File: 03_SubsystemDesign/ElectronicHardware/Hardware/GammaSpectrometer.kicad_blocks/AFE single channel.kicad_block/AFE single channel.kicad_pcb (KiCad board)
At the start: 4 copper layers, 29 parts, among them U2101 OPA690xDBV, U2102 AD8139

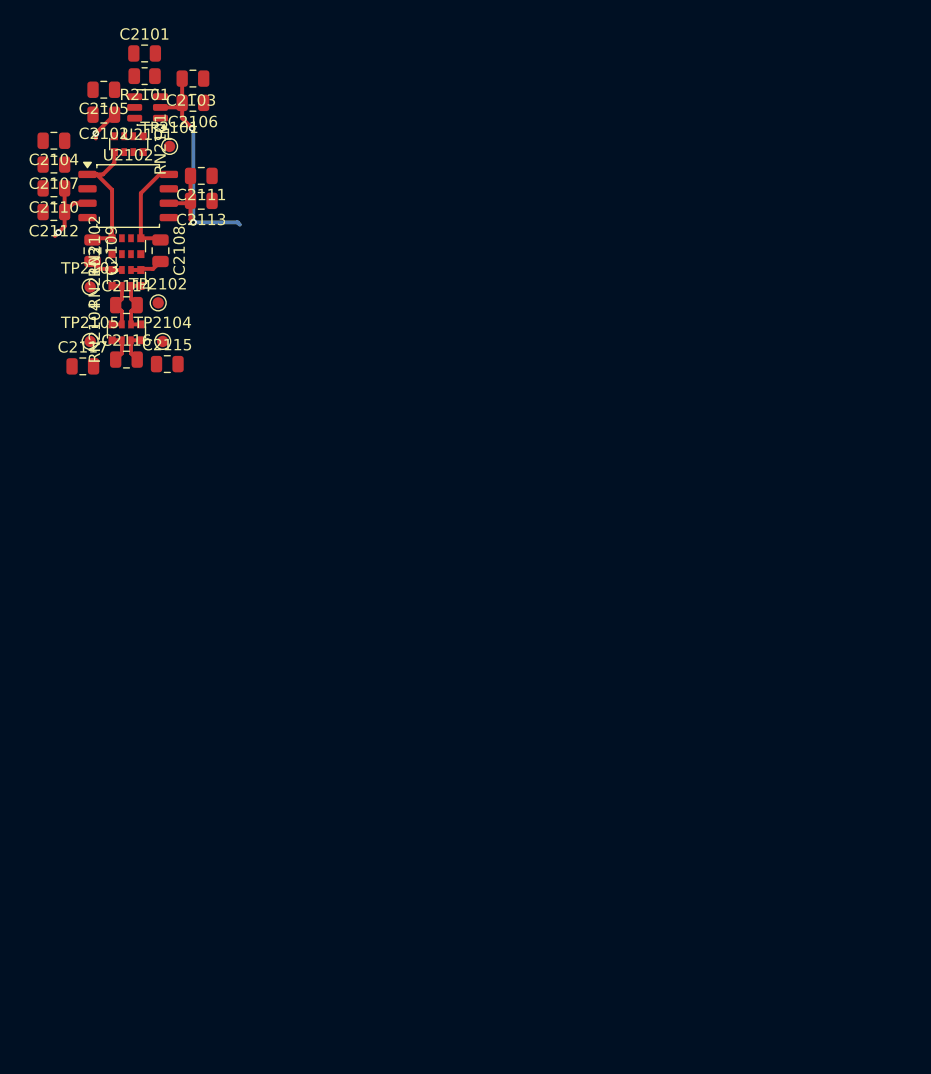
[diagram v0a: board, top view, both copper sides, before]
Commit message: improve CAD folder structure and PCB
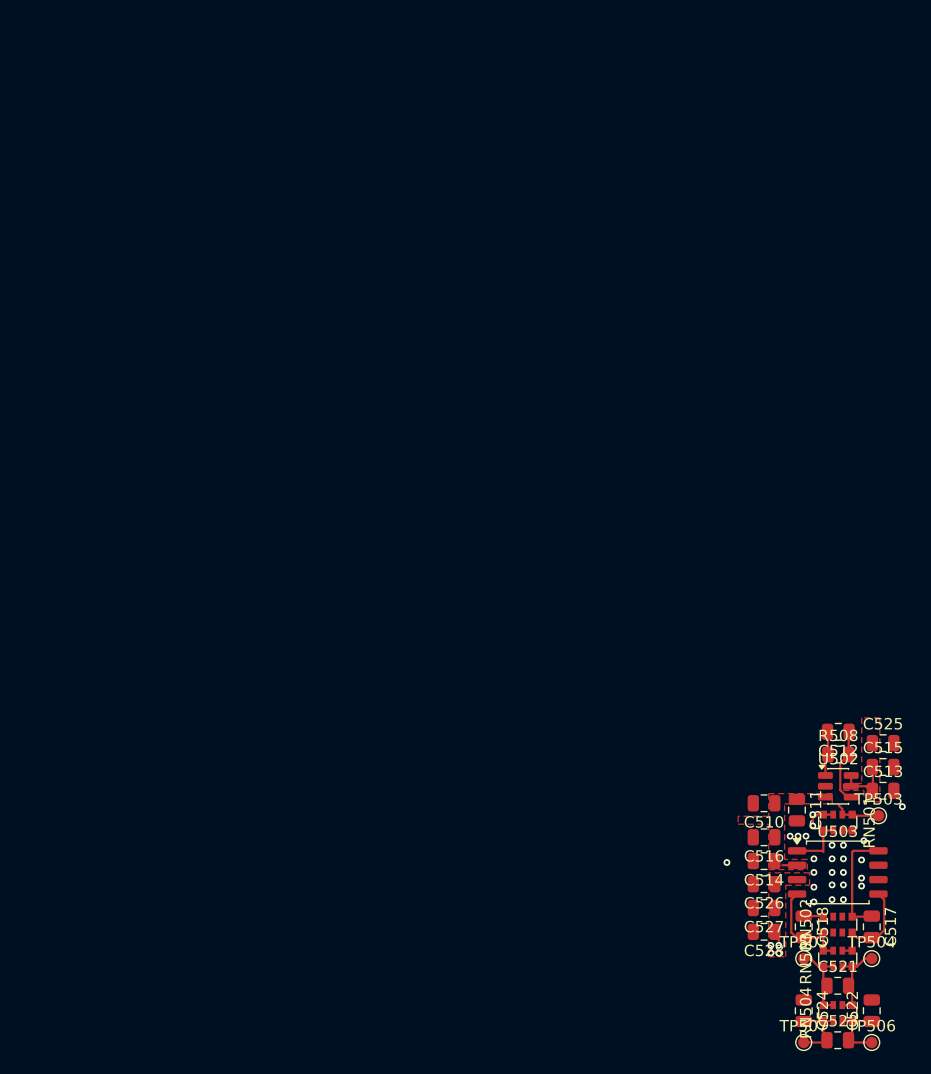
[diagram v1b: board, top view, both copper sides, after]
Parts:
- removed C2101: 33p, Capacitor_SMD:C_0805_2012Metric
- removed C2102, C2103, C2104, C2110, C2111: 100n, Capacitor_SMD:C_0805_2012Metric
- removed C2105, C2106, C2107, C2112, C2113: 10n, Capacitor_SMD:C_0805_2012Metric
- removed C2108, C2109: 1p, Capacitor_SMD:C_0805_2012Metric
- removed C2114: 22p, Capacitor_SMD:C_0805_2012Metric
- removed C2115, C2116, C2117: TBD, Capacitor_SMD:C_0805_2012Metric
- removed R2101: 10k, Resistor_SMD:R_0805_2012Metric
- removed RN2101, RN2102: 1k, Resistor_SMD:R_Array_Convex_4x0612
- removed RN2103, RN2104: 100R, Resistor_SMD:R_Array_Convex_4x0612
- removed TP2101, TP2102, TP2103, TP2104, TP2105: TestPoint, TestPoint:TestPoint_Pad_D1.0mm
- removed U2101: OPA690xDBV, Package_TO_SOT_SMD:SOT-23-6
- removed U2102: AD8139, Package_SO:SOIC-8_5.3x5.3mm_P1.27mm
- added C510: C, Capacitor_SMD:C_0805_2012Metric, F.Cu at (181.6, 98.8)
- added C511: C, Capacitor_SMD:C_0805_2012Metric, F.Cu at (184.5, 99.4)
- added C512: 2n2, Capacitor_SMD:C_0805_2012Metric, F.Cu at (188.2, 92.5)
- added C513: 1u, Capacitor_SMD:C_0805_2012Metric, F.Cu at (192.1, 97.7)
- added C514: C, Capacitor_SMD:C_0805_2012Metric, F.Cu at (181.6, 103.9)
- added C515: 100n, Capacitor_SMD:C_0805_2012Metric, F.Cu at (192.1, 95.6)
- added C516: C, Capacitor_SMD:C_0805_2012Metric, F.Cu at (181.6, 101.8)
- added C517: C, Capacitor_SMD:C_0805_2012Metric, F.Cu at (191.1, 109.7)
- added C518: C, Capacitor_SMD:C_0805_2012Metric, F.Cu at (185.1, 109.7)
- added C521: 150p, Capacitor_SMD:C_0805_2012Metric, F.Cu at (188.1, 114.9)
- added C522: 100p, Capacitor_SMD:C_0805_2012Metric, F.Cu at (191.1, 117.1)
- added C523: 100p, Capacitor_SMD:C_0805_2012Metric, F.Cu at (188.1, 119.7)
- added C524: 100p, Capacitor_SMD:C_0805_2012Metric, F.Cu at (185.1, 117.1)
- added C525: 10n, Capacitor_SMD:C_0805_2012Metric, F.Cu at (192.1, 93.5)
- added C526: 1u, Capacitor_SMD:C_0805_2012Metric, F.Cu at (181.6, 106.0)
- added C527: 100n, Capacitor_SMD:C_0805_2012Metric, F.Cu at (181.6, 108.1)
- added C528: 10n, Capacitor_SMD:C_0805_2012Metric, F.Cu at (181.6, 110.2)
- added R508: 2k, Resistor_SMD:R_0805_2012Metric, F.Cu at (188.2, 94.5)
- added RN501: 1k, Resistor_SMD:R_Array_Convex_4x0612, F.Cu at (188.1, 100.5)
- added RN502: 620R, Resistor_SMD:R_Array_Convex_4x0612, F.Cu at (188.1, 109.5)
- added RN503: 100R, Resistor_SMD:R_Array_Convex_4x0612, F.Cu at (188.1, 112.5)
- added RN504: 100R, Resistor_SMD:R_Array_Convex_4x0612, F.Cu at (188.1, 117.3)
- added TP503: TestPoint, TestPoint:TestPoint_Pad_D1.0mm, F.Cu at (191.7, 99.9)
- added TP504: TestPoint, TestPoint:TestPoint_Pad_D1.0mm, F.Cu at (191.1, 112.5)
- added TP505: TestPoint, TestPoint:TestPoint_Pad_D1.0mm, F.Cu at (185.1, 112.5)
- added TP506: TestPoint, TestPoint:TestPoint_Pad_D1.0mm, F.Cu at (191.1, 119.9)
- added TP507: TestPoint, TestPoint:TestPoint_Pad_D1.0mm, F.Cu at (185.1, 119.9)
- added U502: LTC6268xS6-10, Package_TO_SOT_SMD:TSOT-23-6, F.Cu at (188.2, 97.3)
- added U503: AD8139, Package_SO:SOIC-8_5.3x5.3mm_P1.27mm, F.Cu at (188.1, 104.9)
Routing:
- net /AFE/-5V0_AFE: track 25.7 -> 0.00 mm, vias 2 -> 0
- net Net-(RN2101-R3.2): track 12.3 -> 0.00 mm
- net Net-(RN501-R1.2): track 0.00 -> 10.3 mm
- net /ADC/+5V0_ADC: track 9.67 -> 0.00 mm, vias 2 -> 0
- net Net-(RN502-R1.1): track 0.00 -> 9.28 mm
- net Net-(RN502-R4.1): track 0.00 -> 9.18 mm
- net Net-(RN2101-R1.2): track 8.92 -> 0.00 mm
- net /AFE/+5V0_A: track 0.00 -> 7.83 mm, vias 0 -> 4
- net Net-(RN501-R1.1): track 0.00 -> 7.75 mm
- net Net-(RN503-R1.1): track 0.00 -> 7.43 mm
- net Net-(RN503-R3.1): track 0.00 -> 7.43 mm
- net Net-(RN501-R3.2): track 0.00 -> 6.73 mm
- net /ADC/AFE_OUT_CH2_P: track 0.00 -> 6.59 mm
- net /ADC/AFE_OUT_CH2_N: track 0.00 -> 6.59 mm
- net (no net): track 0.00 -> 6.31 mm, vias 0 -> 1
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- added copper zone on F.Cu, net /AFE/+5V0_A
- added copper zone on In1.Cu, net /AFE/+5V0_A
- added copper zone on F.Cu, net /AFE/AFEChannel1/1V5_REF
- removed copper zone on In1.Cu, net /ADC/+5V0_ADC
- removed copper zone on In1.Cu, net /AFE/-5V0_AFE
